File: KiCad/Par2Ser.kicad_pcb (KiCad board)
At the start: 4 copper layers, 47 x 50 mm, 37 parts, among them J1 DB25_Male, J2 USB_C_Receptacle_USB2.0, J3 Conn_02x05_Odd_Even, U1 LC4032V-5TN48C, U2 FT240XS-R

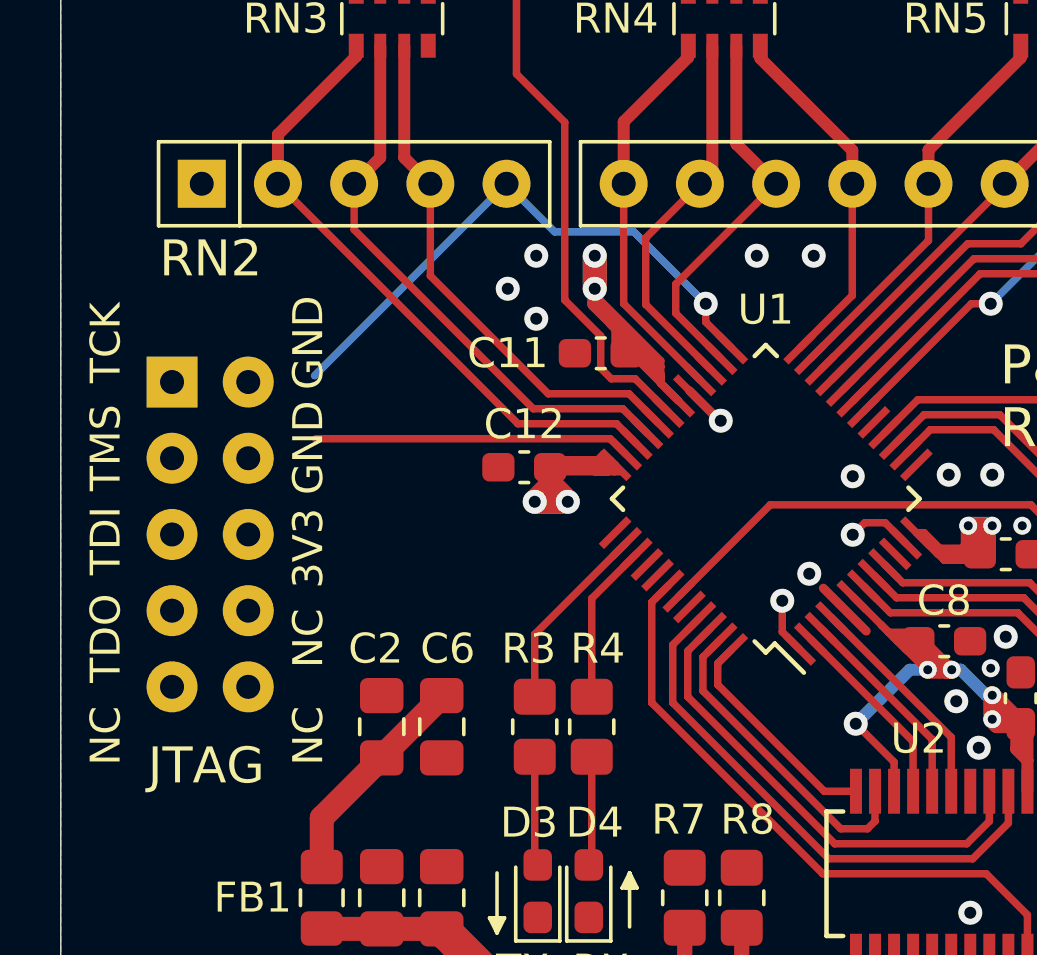
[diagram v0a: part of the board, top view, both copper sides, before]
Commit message: Add 4.7k pull-down resistor on TCK and route all JTAG traces
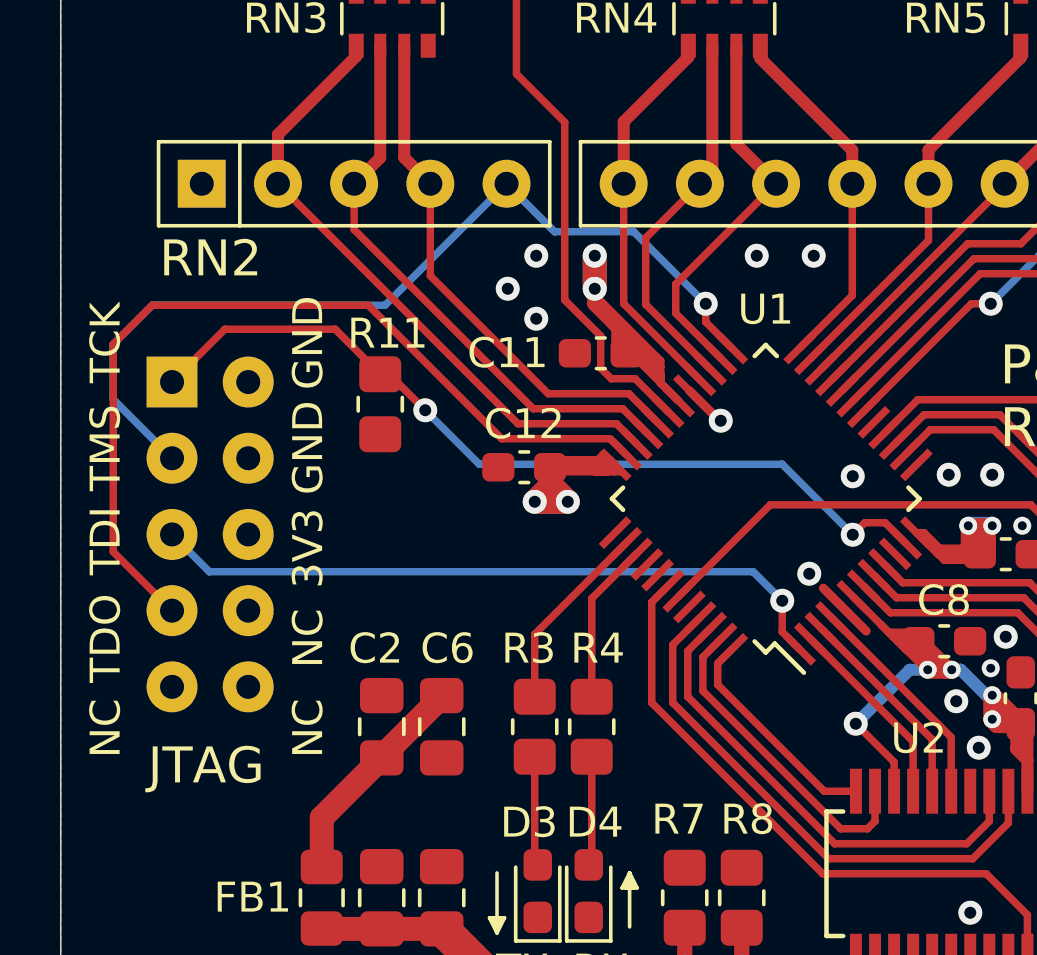
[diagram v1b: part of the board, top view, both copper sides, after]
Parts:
- added R11: 4.7k, Resistor_SMD:R_0805_2012Metric_Pad1.20x1.40mm_HandSolder, F.Cu at (134.7, 106.8)
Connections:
- U1 pad 35: TD0 -> TDO
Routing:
- net TDO: track 0.00 -> 29.4 mm
- net TCK: track 2.22 -> 28.5 mm, vias 1 -> 2
- net TDI: track 1.86 -> 23.1 mm
- net TMS: track 19.2 -> 30.1 mm
- net TD0: track 10.5 -> 0.00 mm

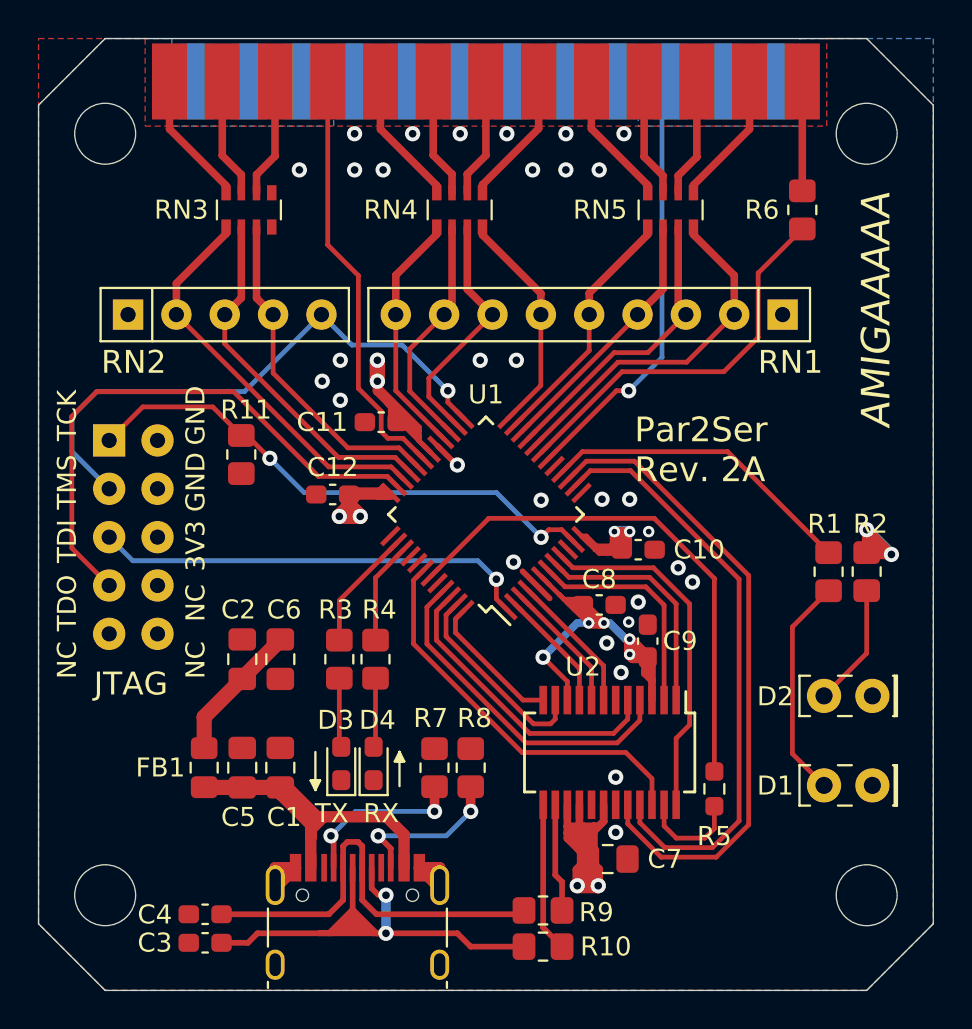
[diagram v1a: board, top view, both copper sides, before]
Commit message: Add 3.3V regulator (TLV75533PDBVR) in SOT-23-5 package and add a 1 uF 0805 decoupling near VOUT pin and complete 3V3 routing and stitching
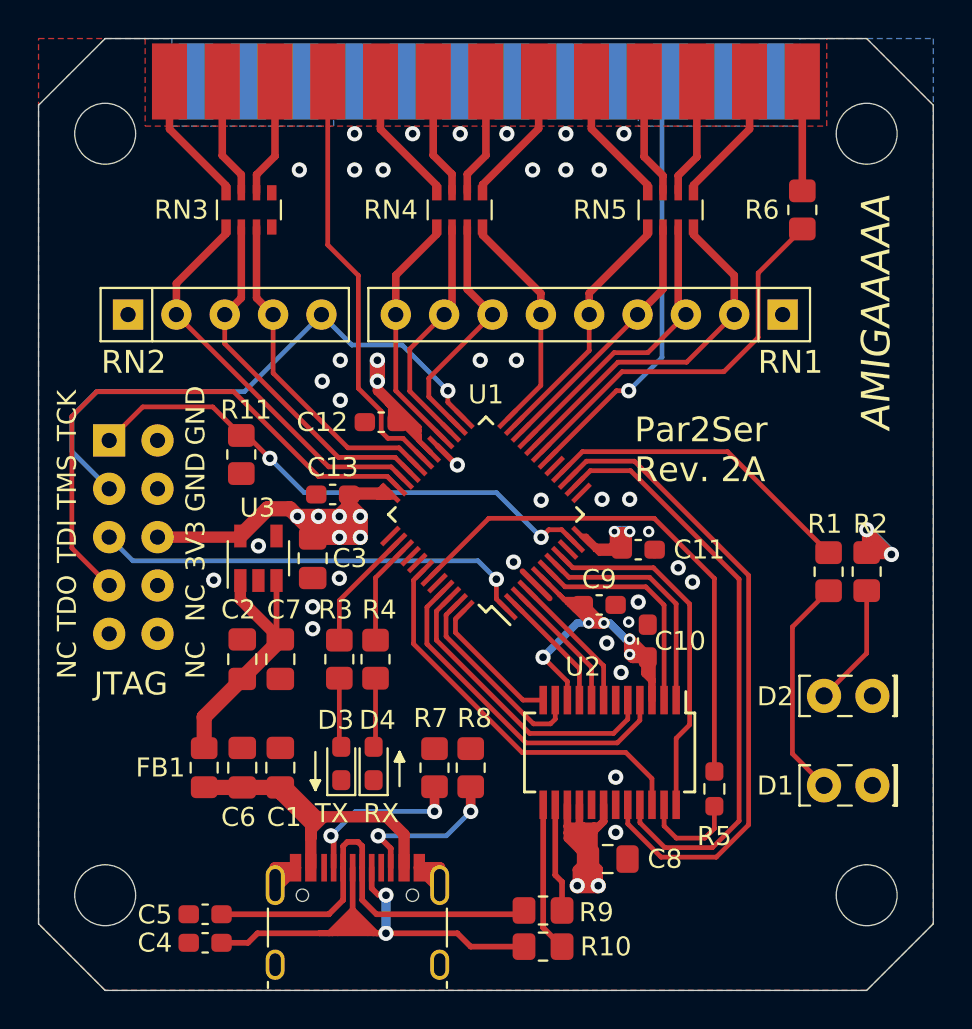
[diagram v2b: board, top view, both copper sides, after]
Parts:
- added C3: 1uF, Capacitor_SMD:C_0805_2012Metric_Pad1.18x1.45mm_HandSolder, F.Cu at (138.4, 112.3)
- added U3: TLV75533PDBVR, Package_TO_SOT_SMD:SOT-23-5, F.Cu at (135.6, 112.3)
- renumbered C9 to C10, C10 to C11, C11 to C12, C12 to C13, C3 to C4, C4 to C5, C5 to C6, C6 to C7, C7 to C8, C8 to C9
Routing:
- net 3V3: track 107.2 -> 134.3 mm, vias 15 -> 19
- net VCC: track 7.37 -> 14.5 mm
- net GND: vias 31 -> 36

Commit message: Silkscreen fixes and add more via stitching
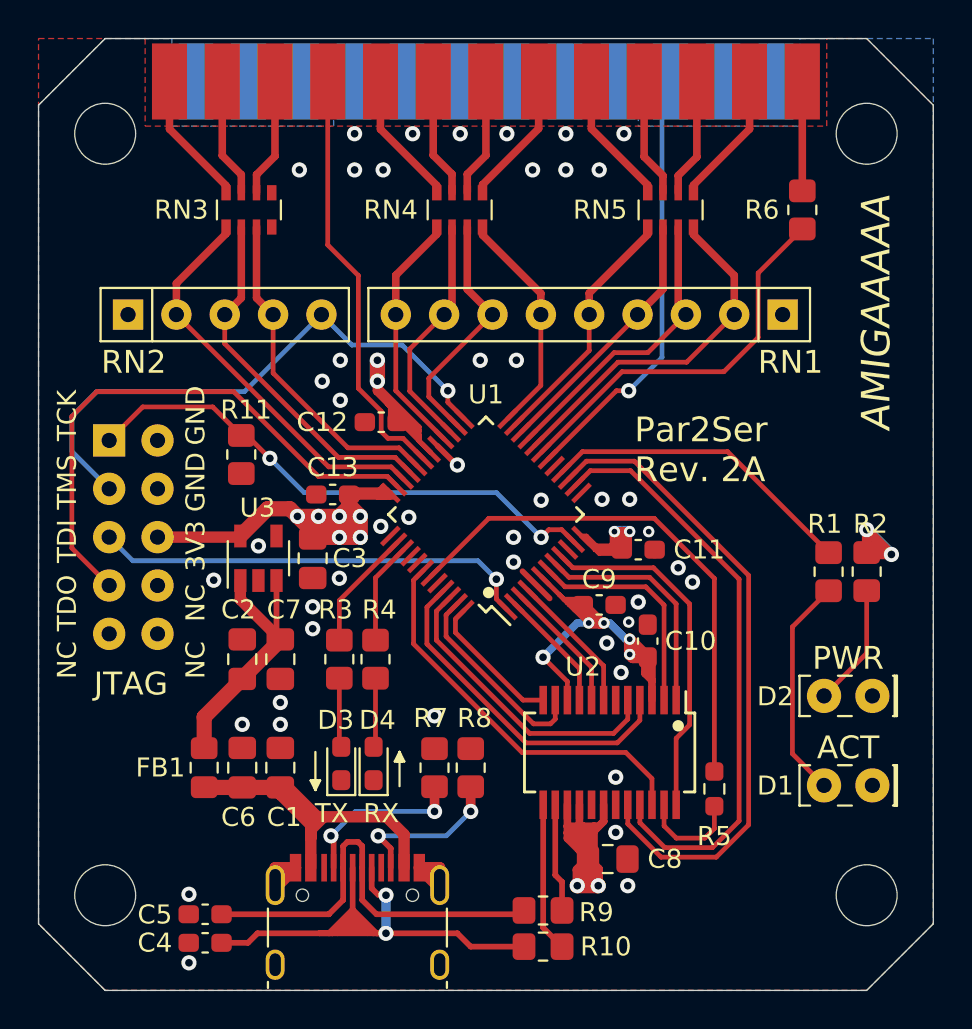
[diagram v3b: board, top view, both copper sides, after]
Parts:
- added REF**: OSHW-Logo_11.4x12mm_SilkScreen, Symbol:OSHW-Logo_11.4x12mm_SilkScreen, B.Cu at (143.8, 118.5)
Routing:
- net GND: vias 36 -> 46
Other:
- board text added: "(C) 2024,2026 Design by J.Bilander"
- board text added: "- +"
- board text added: "ACT"
- board text added: "PWR"
- board text added: "https://github.com/jbilander/Par2Ser"
- board text removed: "(C) 2024 Design by J.Bilander"

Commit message: Add 32 Hz MEMS oscillator (SIT1534AI-H4-DCC-00.032) on clk3 input (pin 42)
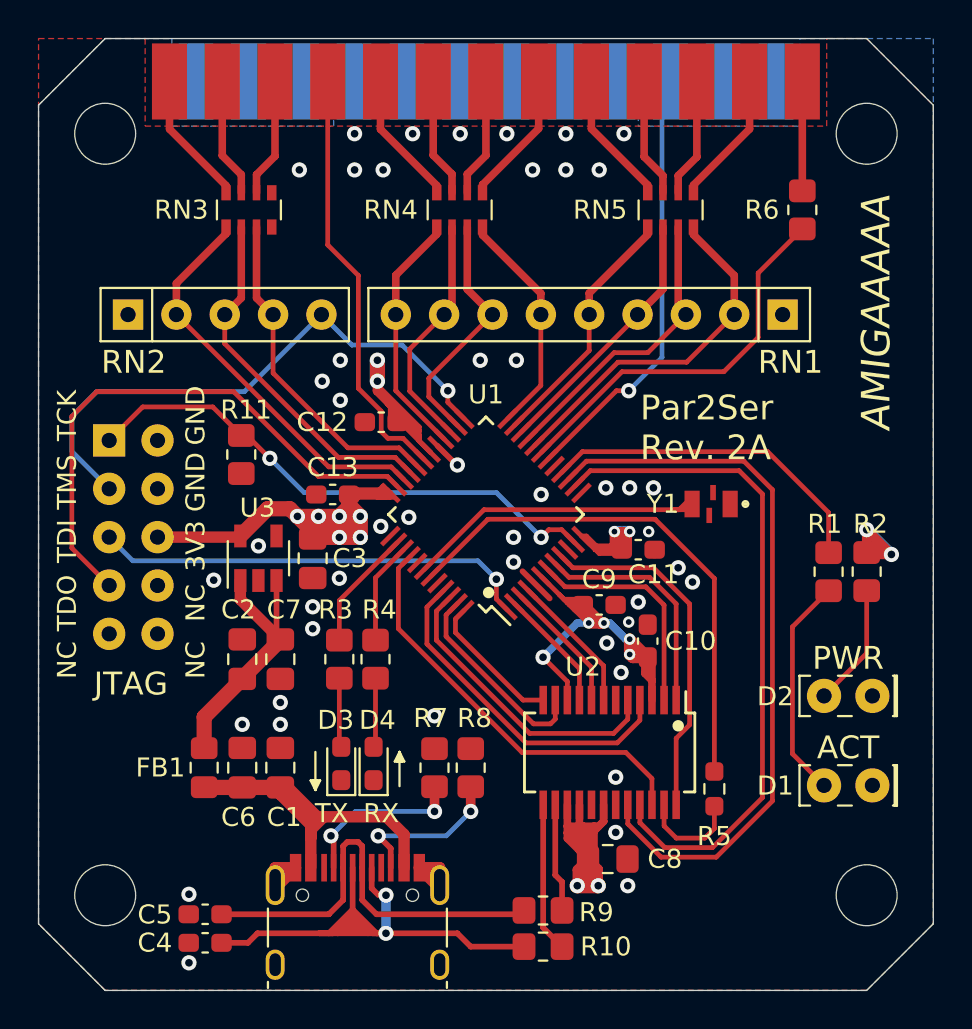
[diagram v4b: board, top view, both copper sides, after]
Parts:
- added Y1: SIT1534AI-H4-DCC-00.032, Par2Ser:SIT1534AIH4DCC00256, F.Cu at (159.3, 109.5)
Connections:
- U1 pad 40: Net-(U1-Pad40) -> CBUS6
- U1 pad 42: CBUS6 -> CLK32Hz
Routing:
- net CLK32Hz: track 0.00 -> 16.8 mm
- net TXE: track 34.2 -> 38.7 mm
- net RXF: track 31.3 -> 35.7 mm
- net ACT_LED: track 16.7 -> 17.9 mm
- net CBUS6: track 20.9 -> 22.0 mm
- net GND: vias 46 -> 47

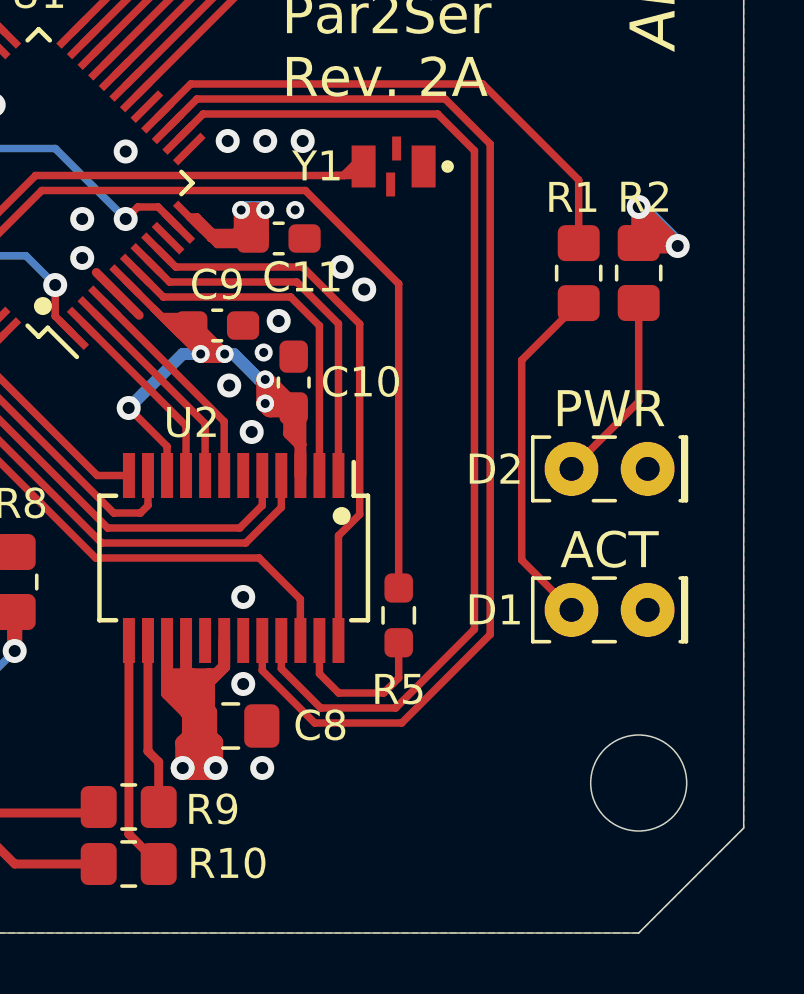
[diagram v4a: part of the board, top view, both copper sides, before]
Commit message: Add decoupling cap and 3.3v supply to MEMS Oscillator
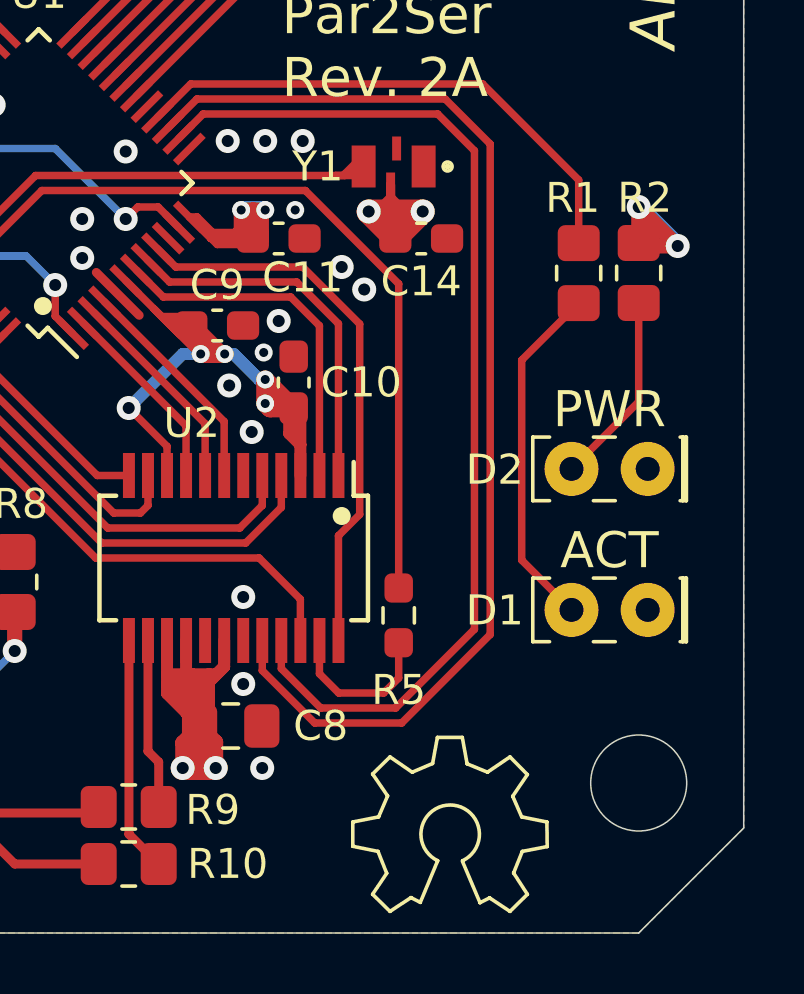
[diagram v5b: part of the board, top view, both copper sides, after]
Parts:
- added C14: 0.1uF, Capacitor_SMD:C_0603_1608Metric_Pad1.08x0.95mm_HandSolder, F.Cu at (160.2, 111.8)
- U1: value LC4032V-5TN48C -> LC4064V-75TN48C
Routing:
- net 3V3: track 134.3 -> 142.9 mm, vias 19 -> 21

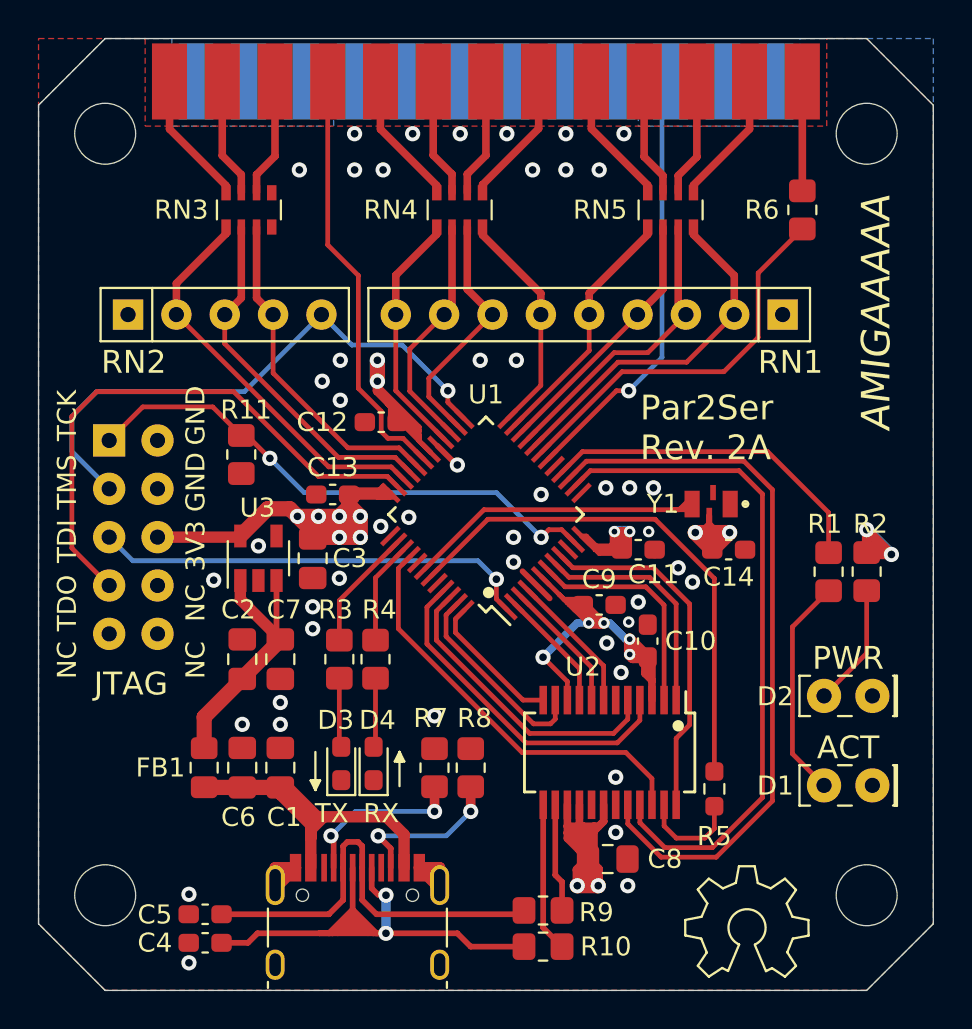
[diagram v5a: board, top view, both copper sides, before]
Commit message: Remove SIT1534 (Y1) slow clock not needed
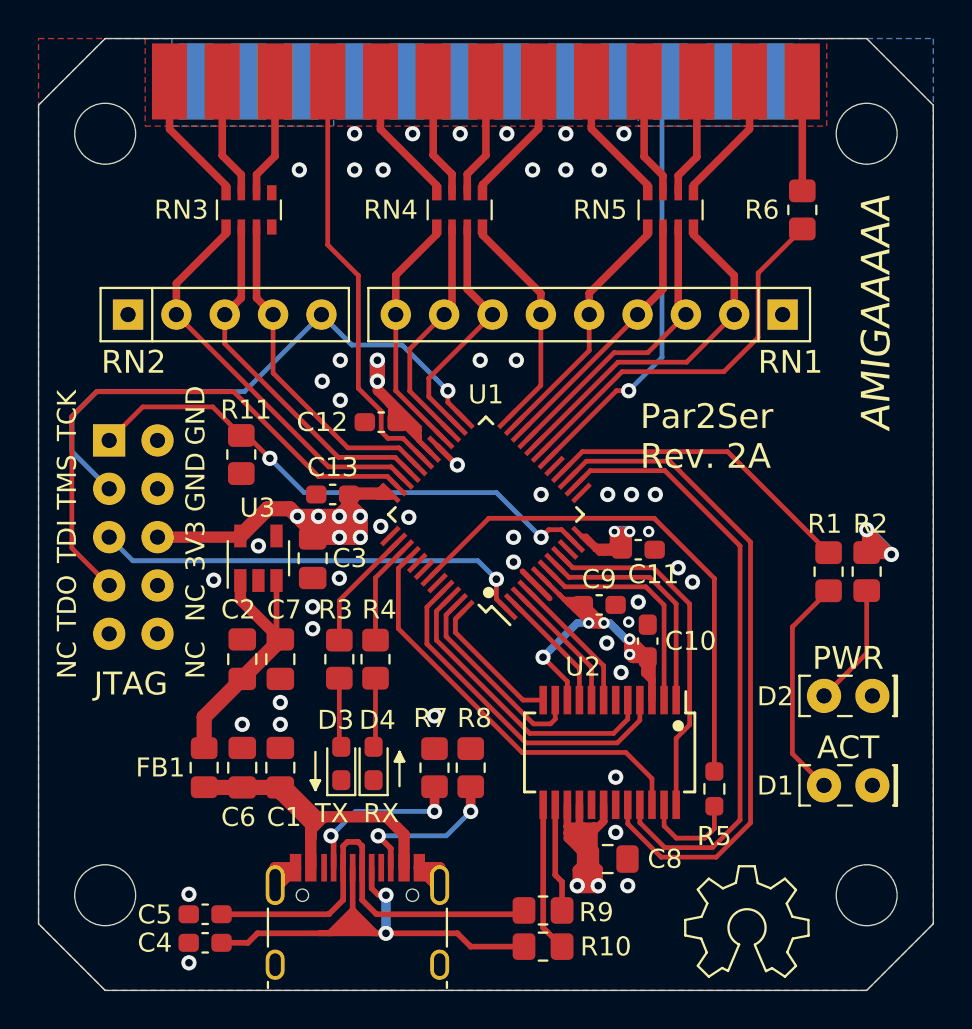
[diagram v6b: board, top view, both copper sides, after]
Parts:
- removed C14: 0.1uF, Capacitor_SMD:C_0603_1608Metric_Pad1.08x0.95mm_HandSolder
- removed Y1: SIT1534AI-H4-DCC-00.032, Par2Ser:SIT1534AIH4DCC00256
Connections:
- U1 pad 42: CLK32Hz -> Net-(U1-Pad42)
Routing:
- net CLK32Hz: track 16.8 -> 0.00 mm
- net 3V3: track 142.9 -> 134.3 mm, vias 21 -> 19
- net RXF: track 35.7 -> 32.4 mm
- net TXE: track 38.7 -> 35.4 mm
- net ACT_LED: track 17.9 -> 16.7 mm
